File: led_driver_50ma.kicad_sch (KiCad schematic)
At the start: 6 parts, among them J1 USB Micro B, J2 Screw_Terminal_01x02, SW2 Slide Switch

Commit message: Use bottom layer ground pour and few other tweaks
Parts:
- C1: footprint Capacitor_SMD:C_0805_2012Metric -> Capacitor_SMD:C_1206_3216Metric
- R1: footprint Resistor_SMD:R_0805_2012Metric -> Resistor_SMD:R_1206_3216Metric
- U1: value ~ -> AL5819
- renumbered SW2 to SW1
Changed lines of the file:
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@@
-	)
-	(junction
-		(at 97.79 96.52)
-		(diameter 0)
-		(color 0 0 0 0)
-	)
-	(junction
-		(at 123.19 96.52)
-		(diameter 0)
-		(color 0 0 0 0)
 	)
 	(junction
@@
 		(color 0 0 0 0)
 	)
-	(junction
-		(at 138.43 96.52)
-		(diameter 0)
-		(color 0 0 0 0)
-	)
-	(junction
-		(at 149.86 96.52)
-		(diameter 0)
-		(color 0 0 0 0)
-	)
 	(wire
 		(pts
@@
 	(wire
 		(pts
-			(xy 138.43 96.52) (xy 149.86 96.52)
-		)
-		(stroke
-			(width 0)
-			(type default)
-		)
-	)
-	(wire
-		(pts
-			(xy 97.79 96.52) (xy 123.19 96.52)
-		)
-		(stroke
-			(width 0)
-			(type default)
-		)
-	)
-	(wire
-		(pts
 			(xy 156.21 80.01) (xy 148.59 80.01)
 		)
@@
 	(wire
 		(pts
-			(xy 138.43 91.44) (xy 138.43 96.52)
-		)
-		(stroke
-			(width 0)
-			(type default)
-		)
-	)
-	(wire
-		(pts
-			(xy 97.79 96.52) (xy 97.79 99.06)
+			(xy 97.79 90.17) (xy 97.79 99.06)
 		)
 		(stroke
@@
 	(wire
 		(pts
-			(xy 123.19 96.52) (xy 138.43 96.52)
-		)
-		(stroke
-			(width 0)
-			(type default)
-		)
-	)
-	(wire
-		(pts
 			(xy 123.19 90.17) (xy 123.19 72.39)
 		)
@@
 	(wire
 		(pts
-			(xy 97.79 90.17) (xy 97.79 96.52)
-		)
-		(stroke
-			(width 0)
-			(type default)
-		)
-	)
-	(wire
-		(pts
-			(xy 138.43 96.52) (xy 138.43 99.06)
+			(xy 138.43 91.44) (xy 138.43 99.06)
 		)
 		(stroke
@@
 	(wire
 		(pts
-			(xy 123.19 95.25) (xy 123.19 96.52)
+			(xy 123.19 95.25) (xy 123.19 99.06)
 		)
 		(stroke
@@
 		(pts
 			(xy 149.86 85.09) (xy 148.59 85.09)
-		)
-		(stroke
-			(width 0)
-			(type default)
-		)
-	)
-	(wire
-		(pts
-			(xy 123.19 96.52) (xy 123.19 99.06)
 		)
 		(stroke
@@
 			)
 		)
-		(property "Value" "~"
-			(at 145.288 72.644 0)
+		(property "Value" "AL5819"
+			(at 139.954 75.184 0)
 			(effects
 				(font
@@
 				)
 				(justify left)
-				(hide yes)
 			)
 		)
@@
 			)
 		)
-		(property "Footprint" "Resistor_SMD:R_0805_2012Metric"
+		(property "Footprint" "Resistor_SMD:R_1206_3216Metric"
 			(at 150.876 92.964 90)
 			(effects
@@
 			)
 		)
-		(property "Footprint" "Capacitor_SMD:C_0805_2012Metric"
+		(property "Footprint" "Capacitor_SMD:C_1206_3216Metric"
 			(at 123.19 92.71 0)
 			(effects
@@
 		(on_board yes)
 		(dnp no)
-		(fields_autoplaced yes)
-		(property "Reference" "SW2"
-			(at 113.03 66.04 0)
+		(property "Reference" "SW1"
+			(at 113.03 69.596 0)
 			(effects
 				(font
@@
 					(size 1.27 1.27)
 				)
+				(hide yes)
 			)
 		)
@@
 			(project "led_driver_50ma"
 				(path "/e3c1330e-065e-4286-90f2-a6a41f035824"
-					(reference "SW2")
-					(unit 1)
-				)
+					(reference "SW1")
+					(unit 1)
+				)

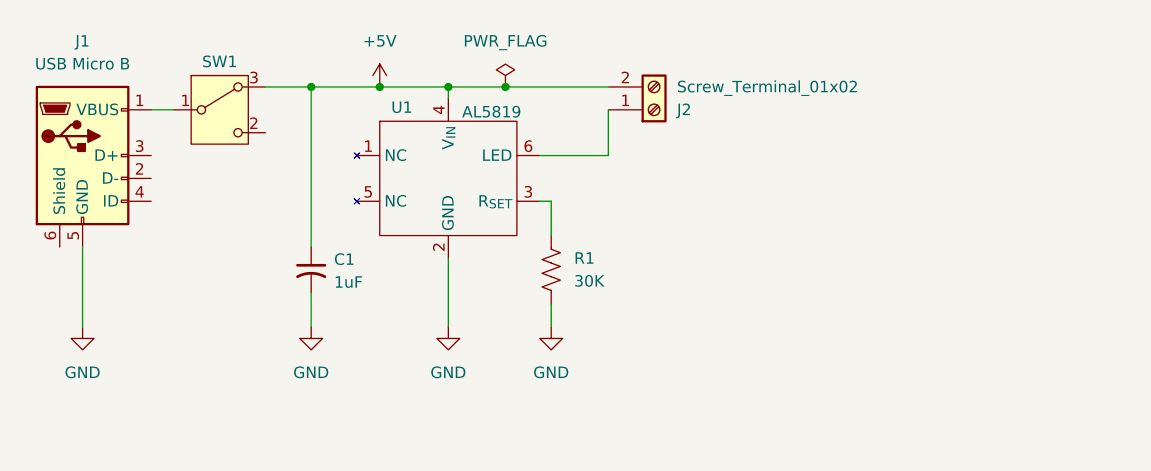
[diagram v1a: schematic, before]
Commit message: switch to USB c instead of usb micro
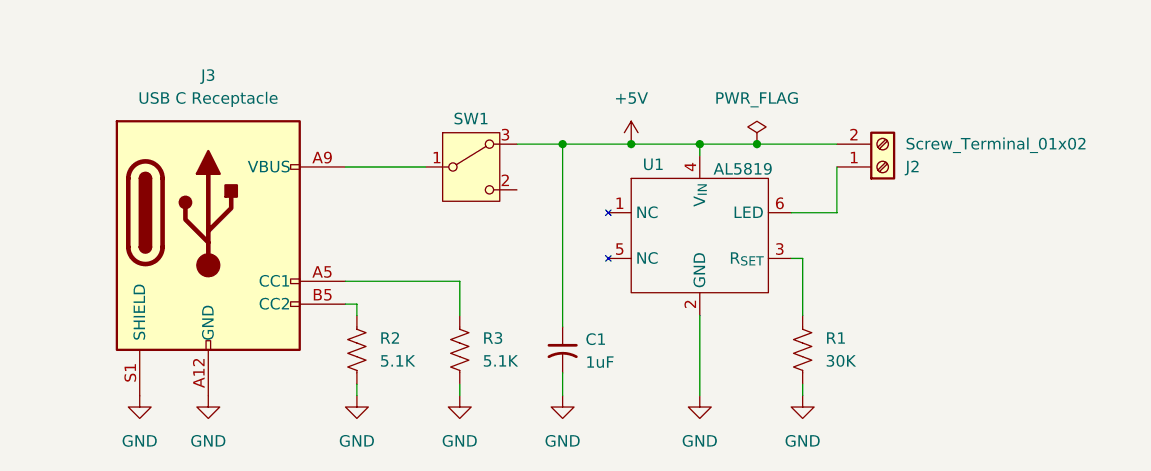
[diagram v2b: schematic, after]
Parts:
- removed J1: USB Micro B, Connector_USB:USB_Micro-B_Amphenol_10118194-0001LF_Horizontal, symbol Connector:USB_B_Micro
- added J3: USB C Receptacle, Connector_USB:USB_C_Receptacle_GCT_USB4125-xx-x_6P_TopMnt_Horizontal, symbol Connector:USB_C_Receptacle_PowerOnly_6P
- added R2, R3: 5.1K, Resistor_SMD:R_1206_3216Metric, symbol Device:R_US
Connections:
- net GND: now also J3.A12 (GND), J3.B12 (GND), J3.S1 (SHIELD), R2.2, R3.2
- net at SW1.1 (B): now also J3.A9 (VBUS), J3.B9 (VBUS)
- new net: J3.B5 (CC2), R2.1
- new net: J3.A5 (CC1), R3.1
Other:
- moved on the sheet: C1, J2, R1, SW1, U1
